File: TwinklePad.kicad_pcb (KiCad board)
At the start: 2 copper layers, 3.6 x 3.3 mm, 54 parts, among them J1 Conn_01x04_Pin, SW1 SW_Push, SW10 SW_Push, SW11 SW_Push, SW12 SW_Push, SW13 SW_Push, SW14 SW_Push, SW15 SW_Push, SW16 SW_Push, SW2 SW_Push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

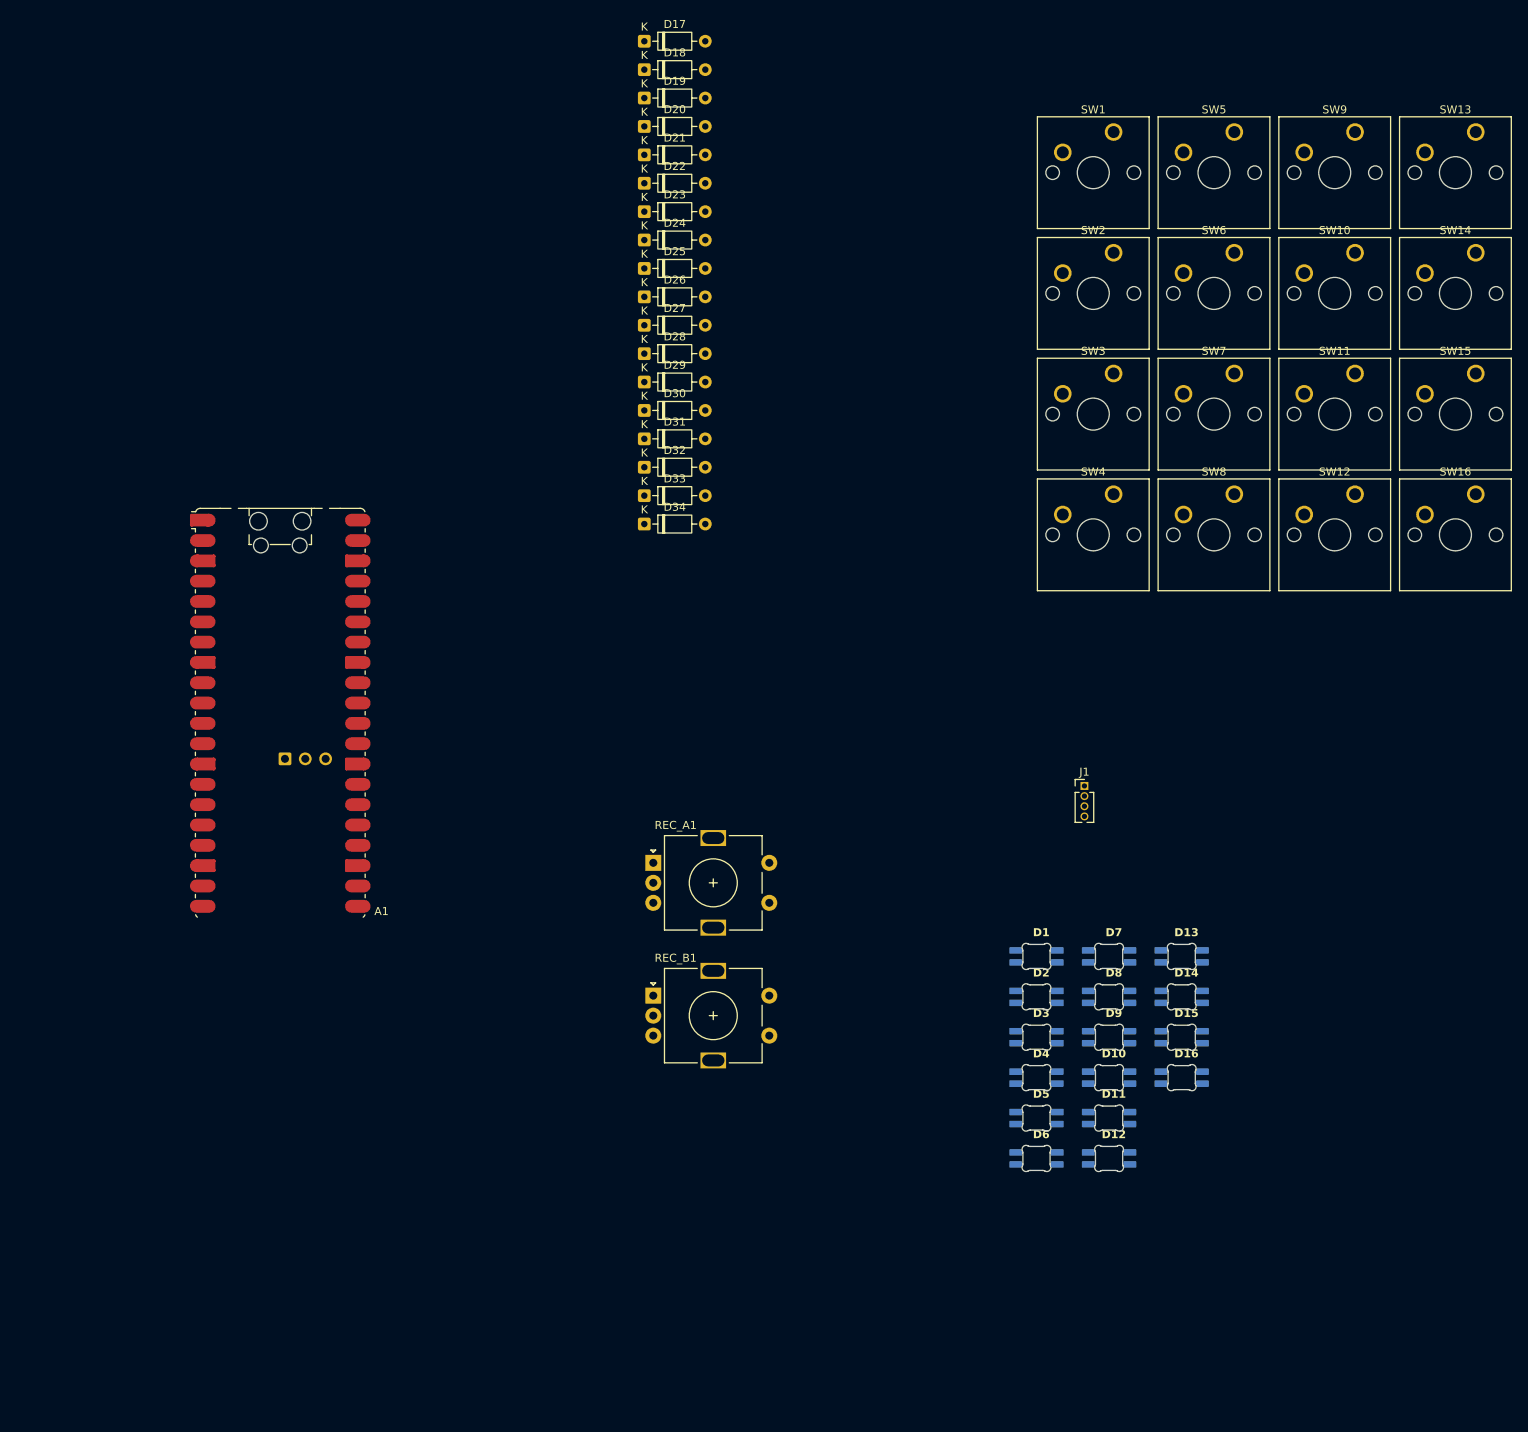
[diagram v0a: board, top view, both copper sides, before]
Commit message: Currently moving keys to layout
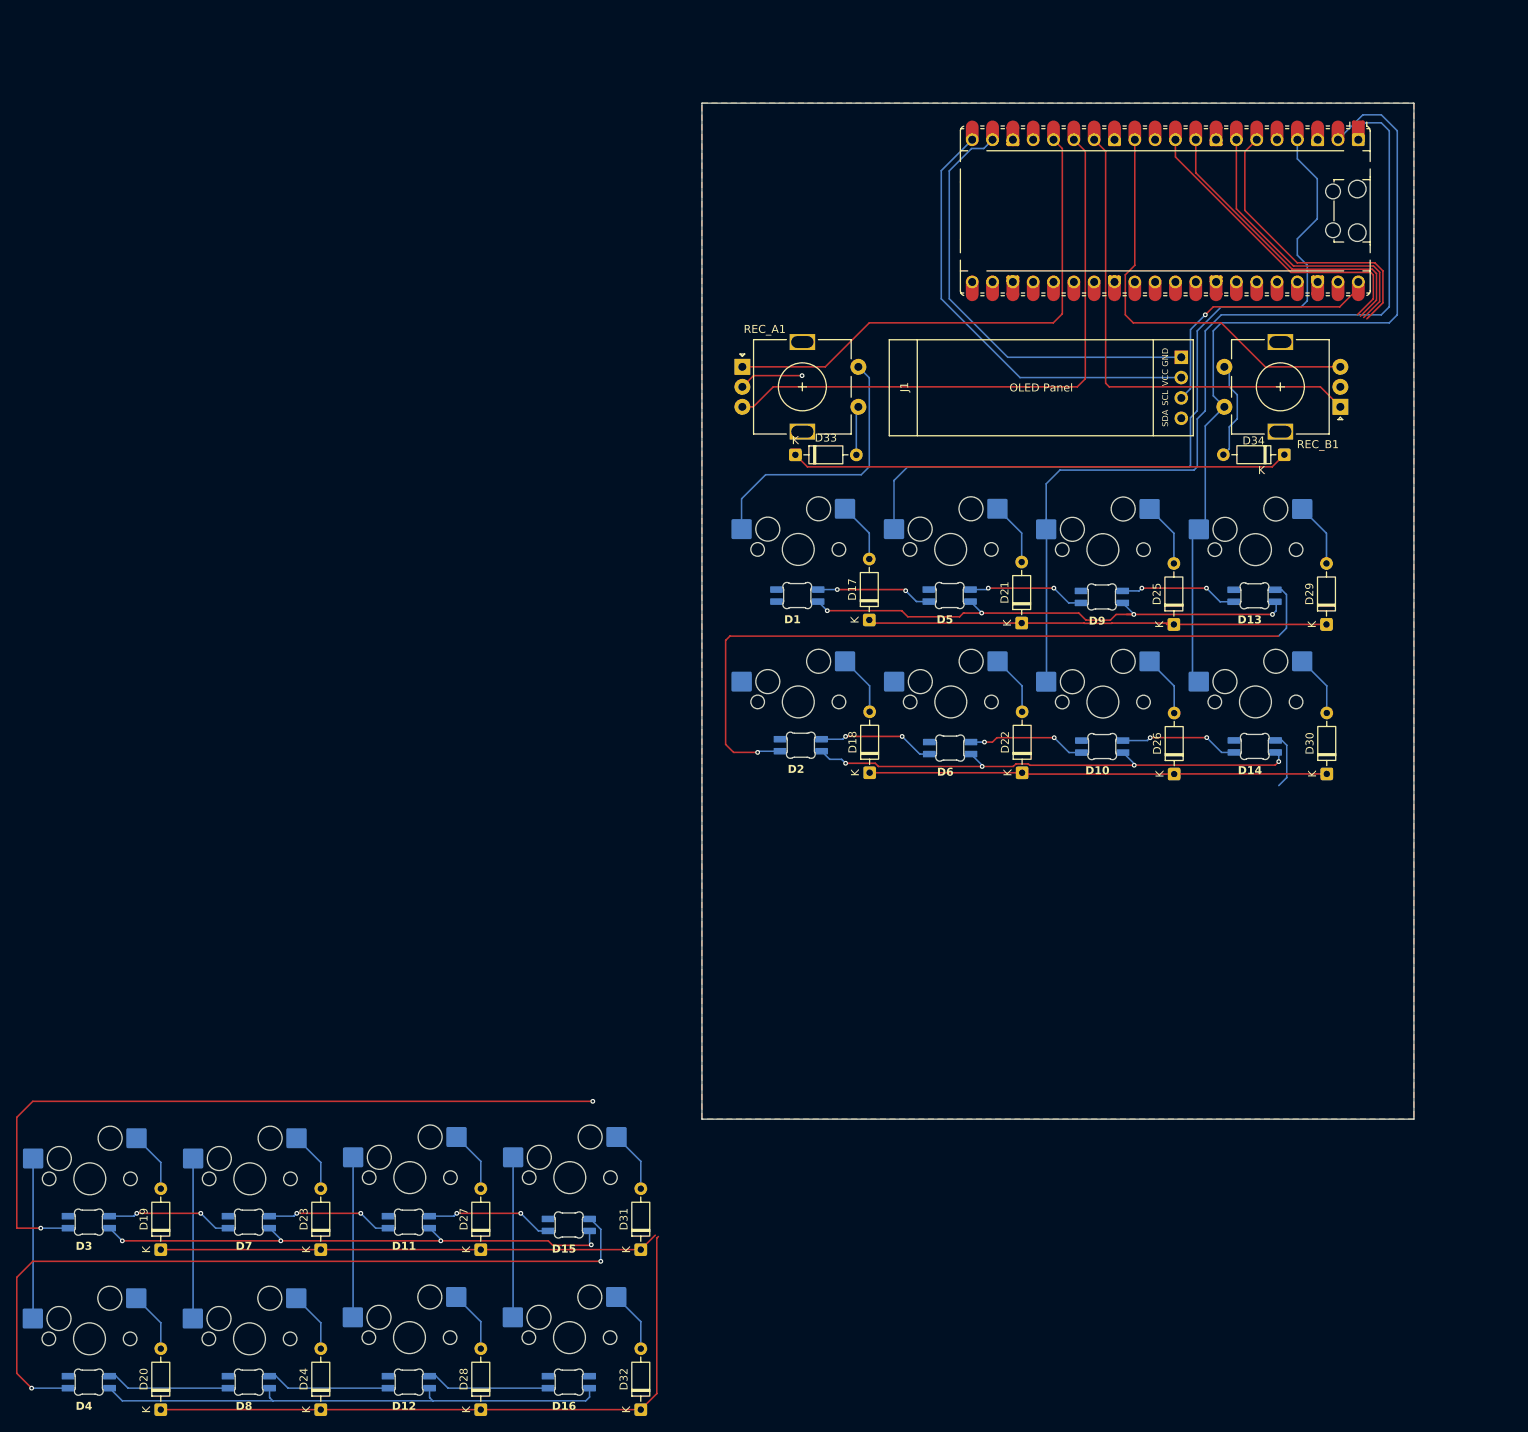
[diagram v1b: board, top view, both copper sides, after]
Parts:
- A1: footprint Module:RaspberryPi_Pico_W_SMD_HandSolder -> Module:RaspberryPi_Pico_Common_Unspecified
- J1: footprint Connector_PinHeader_1.27mm:PinHeader_1x04_P1.27mm_Vertical -> Llama_Other:SSD1306-0.91-OLED-4pin-128x32
- SW1, SW10, SW11, SW12, SW13, SW14, SW15, SW16, SW2, SW3, SW4, SW5, SW6, SW7, SW8, SW9: footprint Button_Switch_Keyboard:SW_Cherry_MX_1.00u_PCB -> Switch_MX_Hotswap:MX-Hotswap-1U; moved to B.Cu
- moved D20 171.4 mm to (34.4, 191.8), turned to 90 degrees
- moved SW4 165.9 mm to (25.5, 183.0), turned to 180 degrees
- moved SW3 162.8 mm to (25.6, 163.0), turned to 180 degrees
- moved SW8 162.2 mm to (45.5, 183.0), turned to 180 degrees
- moved SW7 159.0 mm to (45.6, 163.0), turned to 180 degrees
- moved SW12 158.4 mm to (65.5, 182.8), turned to 180 degrees
- moved D19 156.1 mm to (34.4, 171.8), turned to 90 degrees
- moved SW11 155.1 mm to (65.6, 162.8), turned to 180 degrees
- moved SW16 154.8 mm to (85.5, 182.8), turned to 180 degrees
- moved D24 151.7 mm to (54.4, 191.8), turned to 90 degrees
- moved SW15 151.4 mm to (85.6, 162.8), turned to 180 degrees
- moved D23 135.9 mm to (54.4, 171.8), turned to 90 degrees
- moved D28 133.6 mm to (74.4, 191.8), turned to 90 degrees
- moved A1 127.2 mm to (160.0, 42.0), turned to -90 degrees
- moved D4 124.4 mm to (25.4, 188.3), turned to 180 degrees
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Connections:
- A1 pad 1: COL 0 -> COL 2
- A1 pad 10: ROW 2 -> ROW 1
- A1 pad 11: ROW 3 -> ROW 0
- A1 pad 12: REC_A1 -> REC_B1
- A1 pad 14: REC_A2 -> REC_B2
- A1 pad 15: REC_B1 -> REC_A1
- A1 pad 16: REC_B2 -> REC_A2
- A1 pad 2: COL 1 -> COL 3
- A1 pad 4: COL 2 -> COL 1
- A1 pad 5: COL 3 -> COL 0
- A1 pad 6: COL 4 -> ROW 4
- A1 pad 7: ROW 0 -> ROW 3
- A1 pad 9: ROW 1 -> ROW 2
- D17 pad 1: ROW0 -> ROW 1
- D18 pad 1: ROW1 -> ROW 2
- D19 pad 1: ROW2 -> ROW 3
- D20 pad 1: ROW3 -> ROW 4
- D21 pad 1: ROW0 -> ROW 1
- D22 pad 1: ROW1 -> ROW 2
- D23 pad 1: ROW2 -> ROW 3
- D24 pad 1: ROW3 -> ROW 4
- D25 pad 1: ROW0 -> ROW 1
- D26 pad 1: ROW1 -> ROW 2
- D27 pad 1: ROW2 -> ROW 3
- D28 pad 1: ROW3 -> ROW 4
- D29 pad 1: ROW0 -> ROW 1
- D30 pad 1: ROW1 -> ROW 2
- D31 pad 1: ROW2 -> ROW 3
- D32 pad 1: ROW3 -> ROW 4
- D33 pad 1: ROW0 -> ROW 0
- D33 pad 2: REC_SW_A -> REC_SW_A2
- D34 pad 1: ROW1 -> ROW 0
- D34 pad 2: REC_SW_B -> REC_SW_B2
- REC_A1 pad S2: COL 4 -> COL 0
- REC_B1 pad S2: COL 4 -> COL 3
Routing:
- net VCC: track 0.00 -> 294.9 mm, vias 0 -> 13
- net COL 2: track 0.00 -> 135.4 mm
- net COL 3: track 0.00 -> 122.9 mm
- net COL 1: track 0.00 -> 120.2 mm
- net ROW 4: track 0.00 -> 119.2 mm
- net Net-(D14-DOUT): track 0.00 -> 100.2 mm, vias 0 -> 2
- net Net-(D15-DOUT): track 0.00 -> 98.9 mm, vias 0 -> 2
- net ROW 3: track 0.00 -> 98.9 mm
- net ROW 1: track 0.00 -> 97.2 mm
- net Net-(D13-DOUT): track 0.00 -> 96.9 mm, vias 0 -> 1
- net ROW 2: track 0.00 -> 95.3 mm
- net REC_A1: track 0.00 -> 74.8 mm
- net REC_A2: track 0.00 -> 65.0 mm
- net ROW 0: track 0.00 -> 62.4 mm
- net REC_B2: track 0.00 -> 61.6 mm
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- added copper zone on B.Cu, net GND
- added copper zone on F.Cu, net GND
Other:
- board size 3.6 x 3.3 mm -> 89 x 127 mm
- board text added: "2.4 GHz RF Keep Out"

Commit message: Finished current version of the Twinklepad
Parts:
- moved D20 97.8 mm to (123.0, 150.4)
- moved D4 97.8 mm to (114.0, 146.8)
- moved SW4 97.8 mm to (114.1, 141.5)
- moved D19 97.4 mm to (123.0, 131.3)
- moved D3 97.4 mm to (114.0, 127.8)
- moved SW3 97.4 mm to (114.1, 122.5)
- moved D24 97.0 mm to (142.1, 150.4)
- moved D8 97.0 mm to (133.1, 146.8)
- moved SW8 97.0 mm to (133.2, 141.5)
- moved D7 96.5 mm to (133.0, 127.7)
- moved SW7 96.5 mm to (133.2, 122.4)
- moved D23 96.5 mm to (142.0, 131.3)
- moved D12 96.1 mm to (152.1, 147.0)
- moved D28 96.1 mm to (161.1, 150.5)
- moved SW12 96.1 mm to (152.2, 141.5)
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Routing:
- net VCC: track 294.9 -> 420.5 mm, vias 13 -> 18
- net COL 0: track 55.4 -> 163.7 mm, vias 0 -> 2
- net RGB_DATA: track 0.00 -> 82.3 mm
- net ROW 4: track 119.2 -> 192.9 mm
- net ROW 3: track 98.9 -> 171.6 mm
- net ROW 2: track 95.3 -> 154.3 mm
- net GND: track 8.04 -> 57.4 mm
- net ROW 0: track 62.4 -> 108.4 mm, vias 0 -> 1
- net ROW 1: track 97.2 -> 136.5 mm
- net COL 1: track 120.2 -> 153.2 mm
- net COL 2: track 135.4 -> 153.5 mm
- net COL 3: track 122.9 -> 138.3 mm
- net REC_A1: track 74.8 -> 68.0 mm
- net OLED_SDA: track 55.0 -> 49.8 mm, vias 0 -> 1
- net REC_B1: track 52.0 -> 46.7 mm
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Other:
- board size 89 x 127 mm -> 86 x 124 mm

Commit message: Finished PCB
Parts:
- added J2: Conn_01x02, Connector_PinHeader_2.54mm:PinHeader_1x02_P2.54mm_Vertical, F.Cu at (128.5, 48.5)
- added J3: AudioJack4, Connector_Audio:Jack_3.5mm_PJ320D_Horizontal, F.Cu at (126.0, 35.3)
- added Q1: S8050, Package_TO_SOT_THT:TO-92_Inline, F.Cu at (129.0, 53.5)
- added REF**: MountingHole_3.2mm_M3, MountingHole:MountingHole_3.2mm_M3, F.Cu at (161.8, 132.0)
- added REF**: MountingHole_3.2mm_M3, MountingHole:MountingHole_3.2mm_M3, F.Cu at (123.7, 93.9)
- added REF**: MountingHole_3.2mm_M3, MountingHole:MountingHole_3.2mm_M3, F.Cu at (161.7, 93.9)
- added REF**: MountingHole_3.2mm_M3, MountingHole:MountingHole_3.2mm_M3, F.Cu at (123.6, 131.9)
- added SW17: SW_DP3T, Connector_PinHeader_2.54mm:PinHeader_1x04_P2.54mm_Vertical, F.Cu at (138.4, 74.0)
- REC_A1, REC_B1: footprint HackPad:RotaryEncoder_Alps_EC11E-Switch_Vertical_H20mm -> RotaryEncoder:RotaryEncoder_Alps_EC11E-Switch_Vertical_H20mm
- moved D25 4.58 mm to (161.1, 89.1)
- moved D27 4.31 mm to (161.1, 127.1)
- moved D19 4.19 mm to (123.0, 127.1)
- moved D17 3.83 mm to (123.0, 89.3)
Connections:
- A1 pad 1: COL 2 -> TX
- A1 pad 10: ROW 1 -> ROW 3
- A1 pad 11: ROW 0 -> ROW 2
- A1 pad 12: REC_B1 -> ROW 1
- A1 pad 14: REC_B2 -> ROW 0
- A1 pad 15: REC_A1 -> REC_B1
- A1 pad 16: REC_A2 -> REC_B2
- A1 pad 17: RGB_DATA -> REC_A1
- A1 pad 19: OLED_SDA -> REC_A2
- A1 pad 2: COL 3 -> RX
- A1 pad 20: OLED_SCL -> RGB_DATA
- A1 pad 21: unconnected-(A1-GPIO16-Pad21)_1 -> OLED_SDA
- A1 pad 22: unconnected-(A1-GPIO17-Pad22) -> OLED_SCL
- A1 pad 24: unconnected-(A1-GPIO18-Pad24)_1 -> Buzzer+
- A1 pad 25: unconnected-(A1-GPIO19-Pad25) -> Mode
- A1 pad 26: unconnected-(A1-GPIO20-Pad26) -> Mode 1
- A1 pad 27: unconnected-(A1-GPIO21-Pad27)_1 -> Mode 2
- A1 pad 29: unconnected-(A1-GPIO22-Pad29) -> Mode 3
- A1 pad 4: COL 1 -> COL 3
- A1 pad 5: COL 0 -> COL 2
- A1 pad 6: ROW 4 -> COL 1
- A1 pad 7: ROW 3 -> COL 0
- A1 pad 9: ROW 2 -> ROW 4
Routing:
- net VCC: track 420.5 -> 510.5 mm, vias 18 -> 27
- net TX: track 0.00 -> 64.6 mm
- net RX: track 0.00 -> 58.4 mm, vias 0 -> 2
- net Mode: track 0.00 -> 44.6 mm, vias 0 -> 2
- net GND: track 57.4 -> 16.9 mm, vias 1 -> 6
- net Mode 2: track 0.00 -> 34.5 mm, vias 0 -> 1
- net COL 2: track 153.5 -> 121.0 mm
- net Mode 1: track 0.00 -> 28.9 mm, vias 0 -> 1
- net Mode 3: track 0.00 -> 27.3 mm
- net REC_B1: track 46.7 -> 72.6 mm
- net COL 3: track 138.3 -> 112.5 mm
- net COL 1: track 153.2 -> 128.8 mm
- net ROW 0: track 108.4 -> 131.4 mm, vias 1 -> 3
- net OLED_SCL: track 56.5 -> 33.9 mm, vias 1 -> 3
- net OLED_SDA: track 49.8 -> 32.1 mm, vias 1 -> 3
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
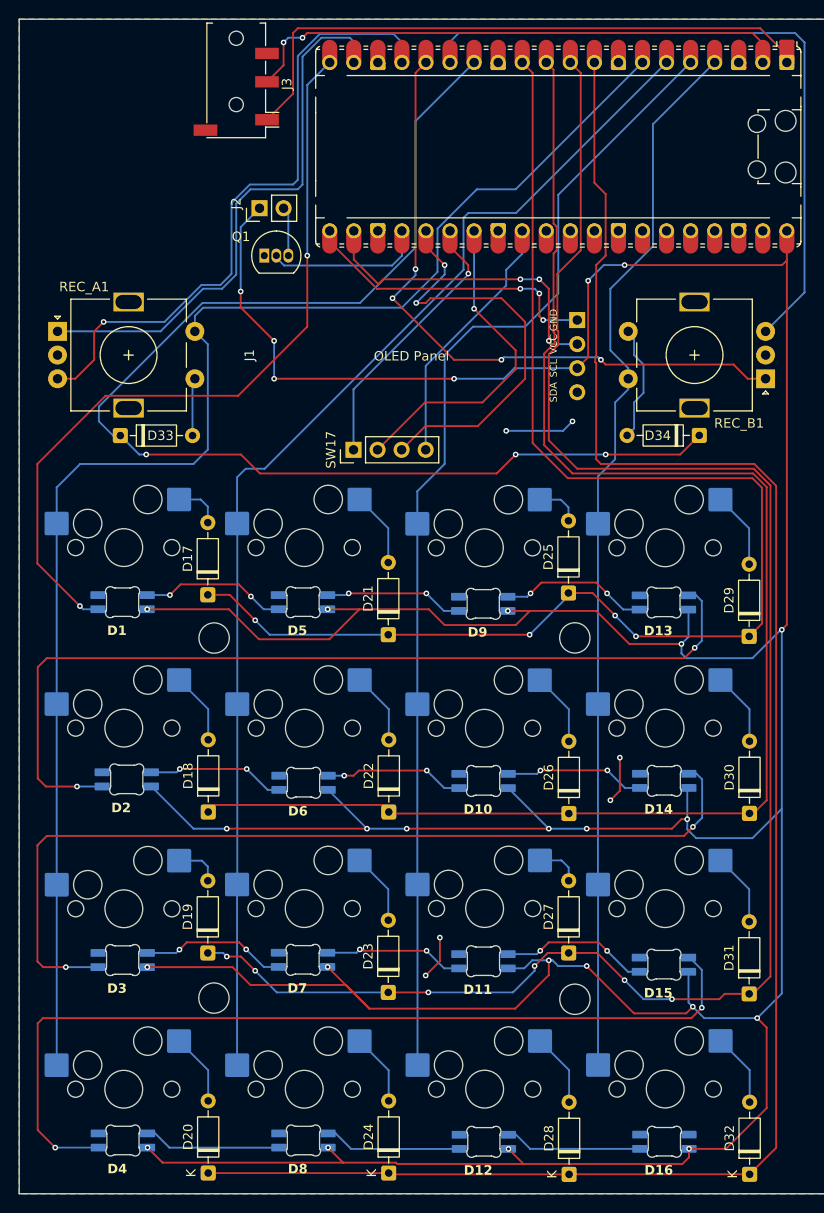
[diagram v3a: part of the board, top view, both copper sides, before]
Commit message: Updated PCB with new models and schematics
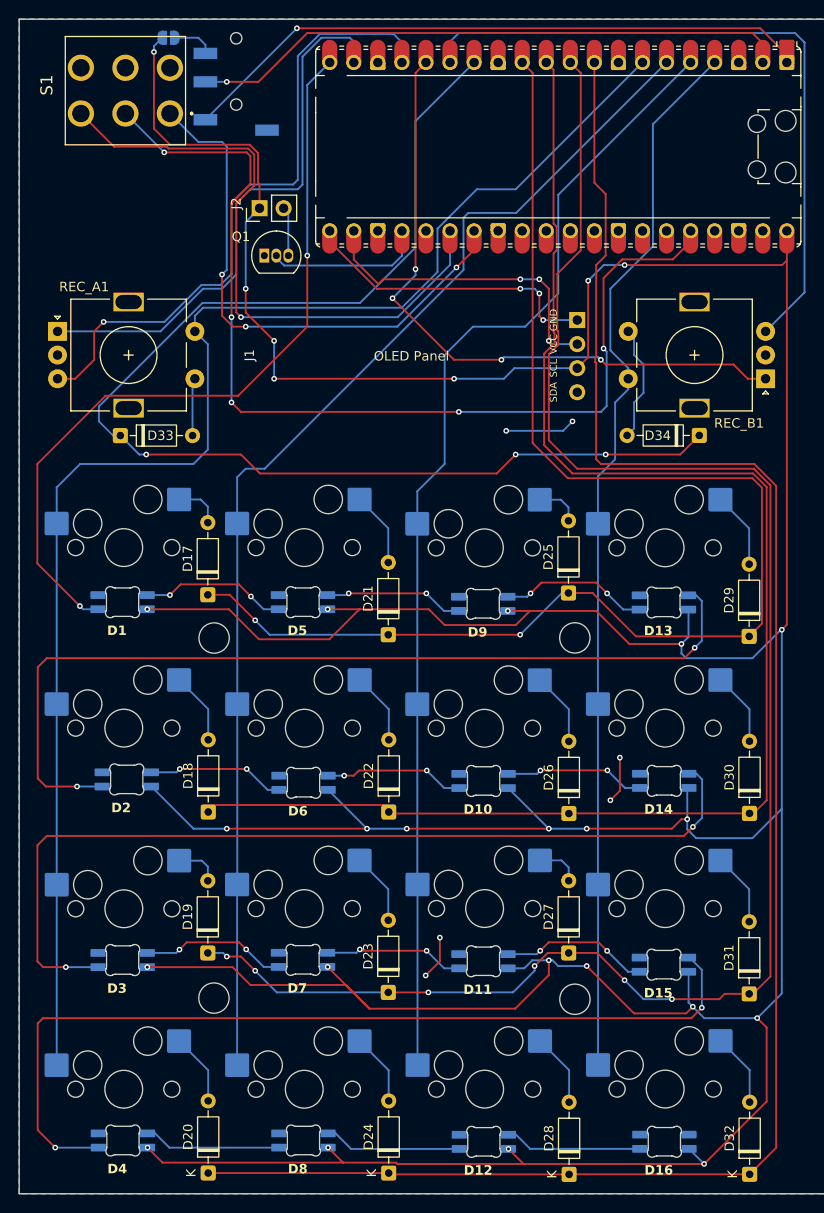
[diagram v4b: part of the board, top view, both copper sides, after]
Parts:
- removed J3: AudioJack4, Connector_Audio:Jack_3.5mm_PJ320D_Horizontal
- removed SW17: SW_DP3T, Connector_PinHeader_2.54mm:PinHeader_1x04_P2.54mm_Vertical
- added J4: PRT-12639, PRT-12639:PRT12639, B.Cu at (126.0, 34.0)
- added JP1: SolderJumper_2_Open, Jumper:SolderJumper-2_P1.3mm_Open_RoundedPad1.0x1.5mm, B.Cu at (118.8, 30.5)
- added S1: 7205P3Y9CQE, Switch_DPDT_2x03:7205P3Y9CQE, F.Cu at (119.0, 38.5)
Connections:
- A1 pad 25: Mode -> unconnected-(A1-GPIO19-Pad25)
- A1 pad 29: Mode 3 -> unconnected-(A1-GPIO22-Pad29)_1
- A1 pad 36: unconnected-(A1-3V3-Pad36) -> +3.3V
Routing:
- net +3.3V: track 0.00 -> 107.7 mm, vias 0 -> 5
- net Mode: track 44.6 -> 0.00 mm, vias 2 -> 0
- net Mode 1: track 28.9 -> 66.2 mm
- net VCC: track 510.5 -> 539.3 mm, vias 27 -> 28
- net Mode 3: track 27.3 -> 0.00 mm
- net Mode 2: track 34.5 -> 58.0 mm, vias 1 -> 3
- net RX: track 58.4 -> 63.4 mm, vias 2 -> 1
- net Net-(JP1-A): track 0.00 -> 4.47 mm
- net TX: track 64.6 -> 67.3 mm, vias 0 -> 1
- net ROW 1: track 145.9 -> 145.7 mm, vias 4 -> 2
